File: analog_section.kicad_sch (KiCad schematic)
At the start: 41 parts, among them J1 Probe +, J2 Probe +, J3 Probe +, J4 Probe +, U1 AD9833xRM, U2 LMH6644MTX, U3 TLV75733PDBV, U4 LMH6643MMX, Y2 25MHz

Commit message: Did some routing
Commiting before changing display from i2c to spi
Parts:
- removed JP3: Jumper_3_Bridged12, Connector_PinHeader_2.54mm:PinHeader_1x03_P2.54mm_Vertical, symbol Jumper:Jumper_3_Bridged12
- removed TP13: TestPoint, TestPoint:TestPoint_Keystone_5000-5004_Miniature, symbol Connector:TestPoint
- removed U3: TLV75733PDBV, Package_TO_SOT_SMD:SOT-23-5, symbol Regulator_Linear:TLV75733PDBV
- added C19: 10n, Capacitor_SMD:C_0603_1608Metric, symbol Device:C
- added JP1: Jumper_2_Open, Connector_PinHeader_2.54mm:PinHeader_1x02_P2.54mm_Vertical, symbol Jumper:Jumper_2_Open
- added R1: 100, Resistor_SMD:R_0603_1608Metric, symbol Device:R
- added R21, R22, R23: 10k, Resistor_SMD:R_0603_1608Metric, symbol Device:R
- added U1: TLV757P, Package_TO_SOT_SMD:SOT-23-5, symbol CustomSymbols:TLV757P
- renumbered C9 to C1, C25 to C15, C1 to C16, C10 to C30, C13 to C31, C14 to C32, C11 to C33, C12 to C34, C15 to C35, C5 to C4, C4 to C5, C8 to C6, D3 to D1, D4 to D2, D2 to D3, J1 to J2, J2 to J3, J3 to J4, J4 to J5, PS2 to PS1, R11 to R10, R13 to R11, R14 to R12, R1 to R2, R2 to R3, R3 to R4, R12 to R9, TP2 to TP1, TP11 to TP2, TP8 to TP3, TP7 to TP4, U1 to U2, U2 to U6, Y2 to Y1
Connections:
- net TST_OP_IN is gone; now on net DDS_HPF: U4.5 (+)
- net +3V3A: now also JP1.2 (B), U1.5 (OUT)
- net +5V: now also U1.1 (IN), U1.3 (EN)
- net DDS_AMPLIFIED: now also U4.7; no longer U4.1
- net DDS_HPF: now also JP1.1 (A); no longer U4.3 (+)
- net DDS_OUT: now also R1.1; no longer C16.1
- net GND: now also C19.2, R21.1, R22.1, R23.1, U1.2 (GND), U1.4 (NC)
- net RANGE_S0: now also R22.2
- net RANGE_S1: now also R21.2
- net TEST_GAIN_S: now also R23.2
- net INV: now reaches R3.1, R4.2
- net INV: now also U4.6 (-); no longer U4.2 (-)
- removed net TST_OP_OUT: U4.6 (-), U4.7
- new net DDS_LPF_1: C19.1, R1.2, U4.3 (+)
- new net DDS_LPF_2: C16.1, U4.1, U4.2 (-)
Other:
- note added: "LPF to remove noise fc = 159KHz"
- note added: "There are some digital signals for the range resistors and DDS that need to be present in the analog section. However, crosstalk should not be an issue even for close analog and digital traces. This is because the digital traces do not need to change level when the DDS output is on."
- note added: "This jumper can be used to test the output impedance of the amplifier by measuring open circuit vs load voltage at the output"
- note removed: "This opamp can be used to find the output impedance by measuring open circuit vs load voltage at test point"
- moved on the sheet: C1, C15, C16, C2, C3, C4, C5, C6, PS1, R2, R3, R4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

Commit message: Done
Schematics and PCB are "done".
Meaning I've just finished but need to review
the design before it's ready to order.
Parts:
- renumbered R12 to R10, R15 to R13, R21 to R15, R22 to R16, R23 to R17, R9 to R7, R10 to R8, R11 to R9, TP2 to TP4, TP3 to TP5, TP4 to TP6
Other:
- note added: "Analog Power"
- note added: "Opamp Power Suppy Connections"
- note added: "Resistor Switch Pulldowns"
- note removed: "Analog Power Supplies"
- note removed: "There are some digital signals for the range resistors and DDS that need to be present in the analog section. However, crosstalk should not be an issue even for close analog and digital traces. This is because the digital traces do not need to change level when the DDS output is on."
- moved on the sheet: C30, C31, C32, C33, C34, C35, C4, C5, D1, D2, D3, J2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

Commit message: Added polish
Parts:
- added C44: 10u, Capacitor_SMD:C_0603_1608Metric, symbol Device:C
- added C45: 4u7, Capacitor_SMD:C_0603_1608Metric, symbol Device:C
- added D1, D2: LED, LED_SMD:LED_0603_1608Metric, symbol Device:LED
- added R5, R7: 1k, Resistor_SMD:R_0603_1608Metric, symbol Device:R
- J4, J5: value Probe + -> Probe -
- renumbered C15 to C17, C16 to C18, C19 to C21, C34 to C33, C35 to C34, C33 to C35, D1 to D3, D2 to D4, D3 to D5, R15 to R10, R16 to R11, R17 to R12, R8 to R13, R9 to R14, R10 to R16, R13 to R18, R7 to R9
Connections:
- net +3V3A: now also D1.2 (A)
- net +5V: now also C45.1
- net -3V3A: now also C44.1, R7.2
- net GND: now also C44.2, C45.2, D2.2 (A), R5.2
- new net: D1.1 (K), R5.1
- new net: D2.1 (K), R7.1
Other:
- note added: "Don't bother with LPF for digital signals into analog section. Because the digital signals are constant while the DDS outputs the test waveform and the MCU reads samples."
- moved on the sheet: C31, C32, C33, C34, PS1, R10, R11, R12, U4C, U6E

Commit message: Changed range resistor selector design
Changed range resistor selector from an analog mux
to a MOSFET BPS design. This should improve on resistance, linearity,
and temperature stability for the range resistors.
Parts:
- added C29, C40: 1u, Capacitor_SMD:C_0603_1608Metric, symbol Device:C
- added C38, C39: 100n, Capacitor_SMD:C_0603_1608Metric, symbol Device:C
- added C48: 4u7, Capacitor_SMD:C_0603_1608Metric, symbol Device:C
- added PS2: A0512S-1WR2, Converter_DCDC:Converter_DCDC_XP_POWER-IAxxxxS_THT, symbol Converter_DCDC:IA2412S
- added R23, R26: 10k, Resistor_SMD:R_0603_1608Metric, symbol Device:R
- added U9: LM324, Package_SO:SOIC-14_3.9x8.7mm_P1.27mm, symbol Device:Opamp_Quad
- D1, D2: Already Have (none) -> 1
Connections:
- net RANGE_S1 is gone; now on net RANGE_S0: R10.2
- net +3V3: now also R23.2
- net +5V: now also C48.1, PS2.1 (+Vin)
- net GND: now also C29.2, C38.1, C39.2, C40.1, C48.2, PS2.2 (-Vin), PS2.5 (0V), R26.1, U9.12 (+)
- net RANGE_S0: now also U9.10 (+), U9.5 (+)
- net TEST_GAIN_S: now also U9.3 (+)
- new net: U9.13 (-), U9.14
- new net +12V: C29.1, C38.2, PS2.6 (+Vout), U9.4 (V+)
- new net -12V: C39.1, C40.2, PS2.4 (-Vout), U9.11 (V-)
- new net COMP_REF: R23.1, R26.2, U9.2 (-), U9.6 (-), U9.9 (-)
- new net RANGE_G0: U9.7
- new net RANGE_G1: U9.8
- new net TEST_GAIN_G: U9.1
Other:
- sheet Gain Selector ports: added G0; removed S
- sheet Range Resistor 1 ports: added G0, G1; removed S0, S1
- sheet Range Resistor 2 ports: added G0, G1; removed S0, S1
- note added: "Component selection was based on what's cheap. If this were a real lab instrument it should probably use components that don't change with temperature (atleast in the test signal path). Bad tolerances are OK, since the device needs calibration anyway."
- note added: "Range Resistor BPS Gate Driving"
- note removed: "Resistor Switch Pulldowns"
- moved on the sheet: C1, C17, C18, C2, C21, C3, C30, C31, C32, C33, C34, C35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

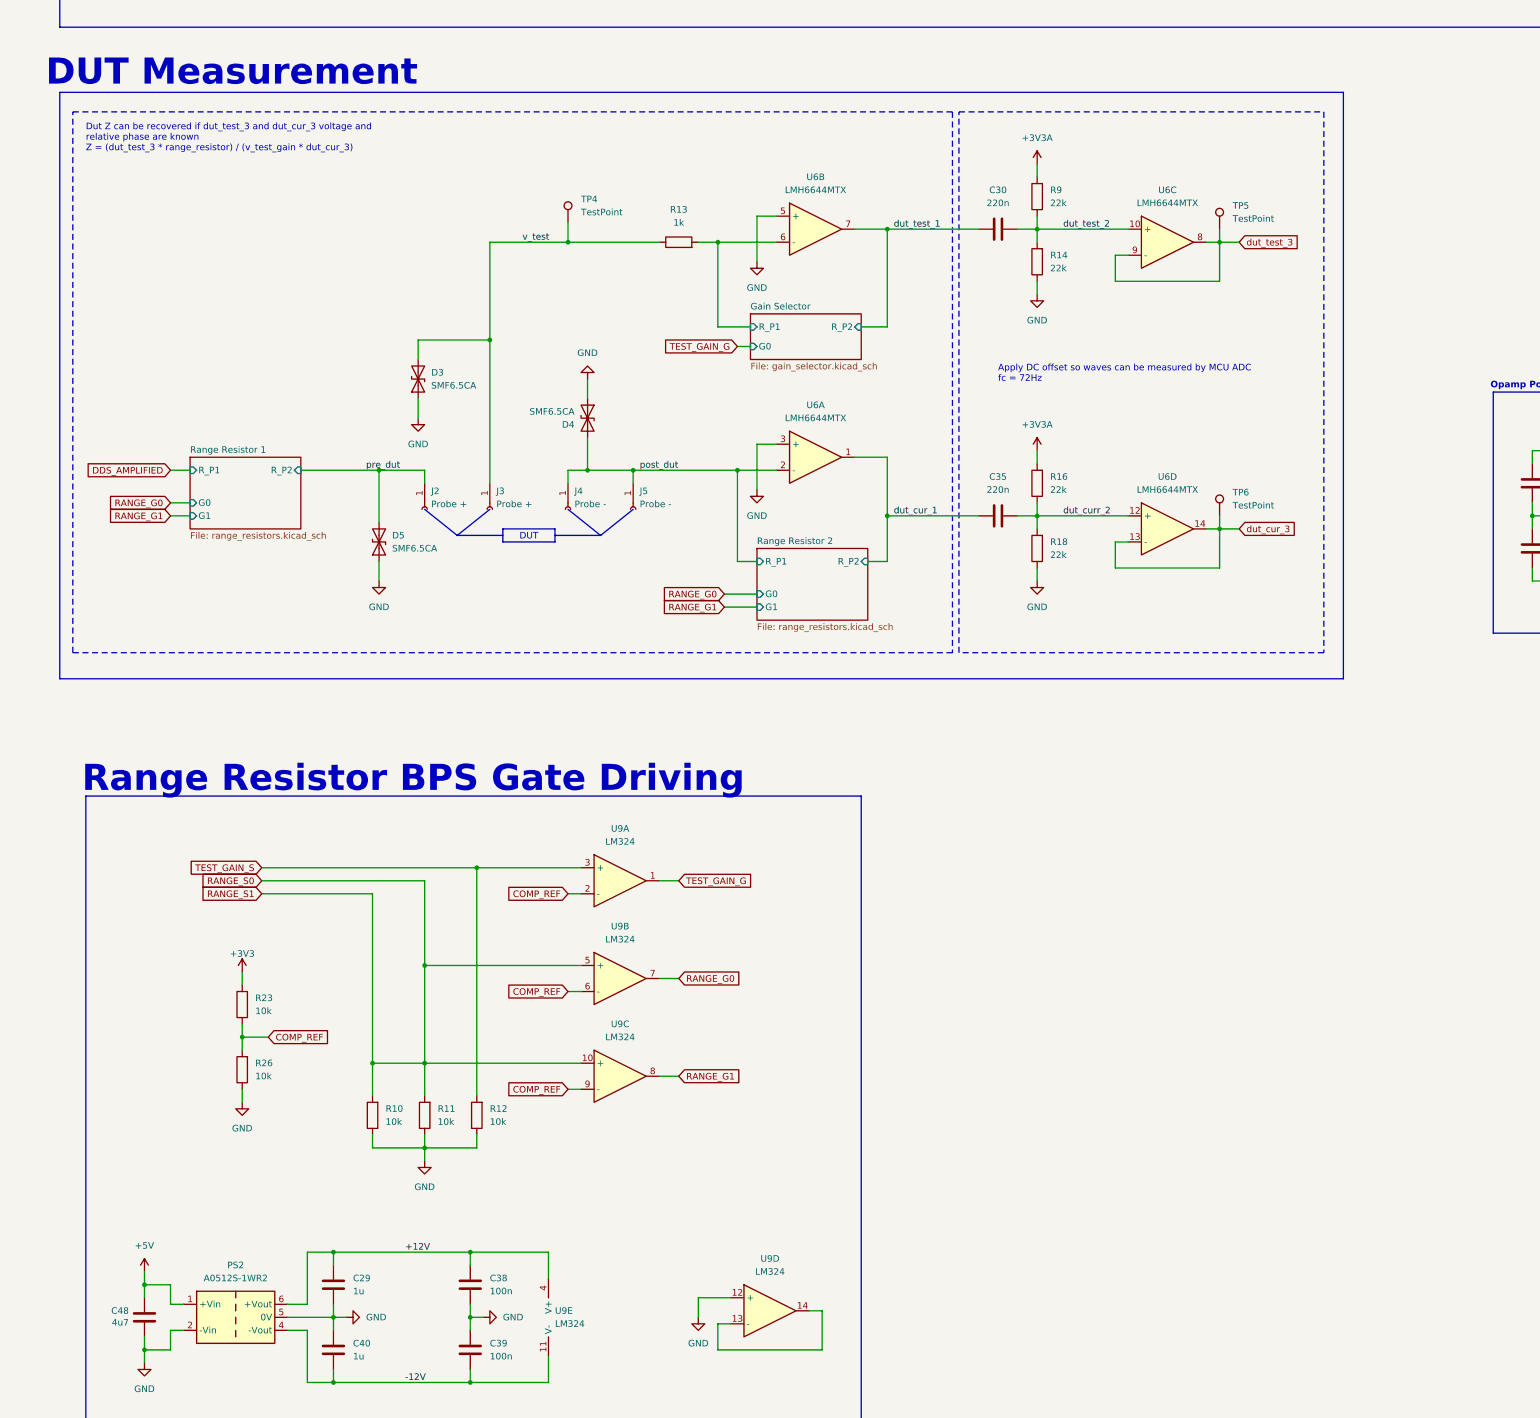
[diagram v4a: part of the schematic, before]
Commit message: Started new layout
Range resistors now use MOSFET BPS.
Currently there's no protection for over voltage on the opamp or mcu
inputs, so that needs to be done.
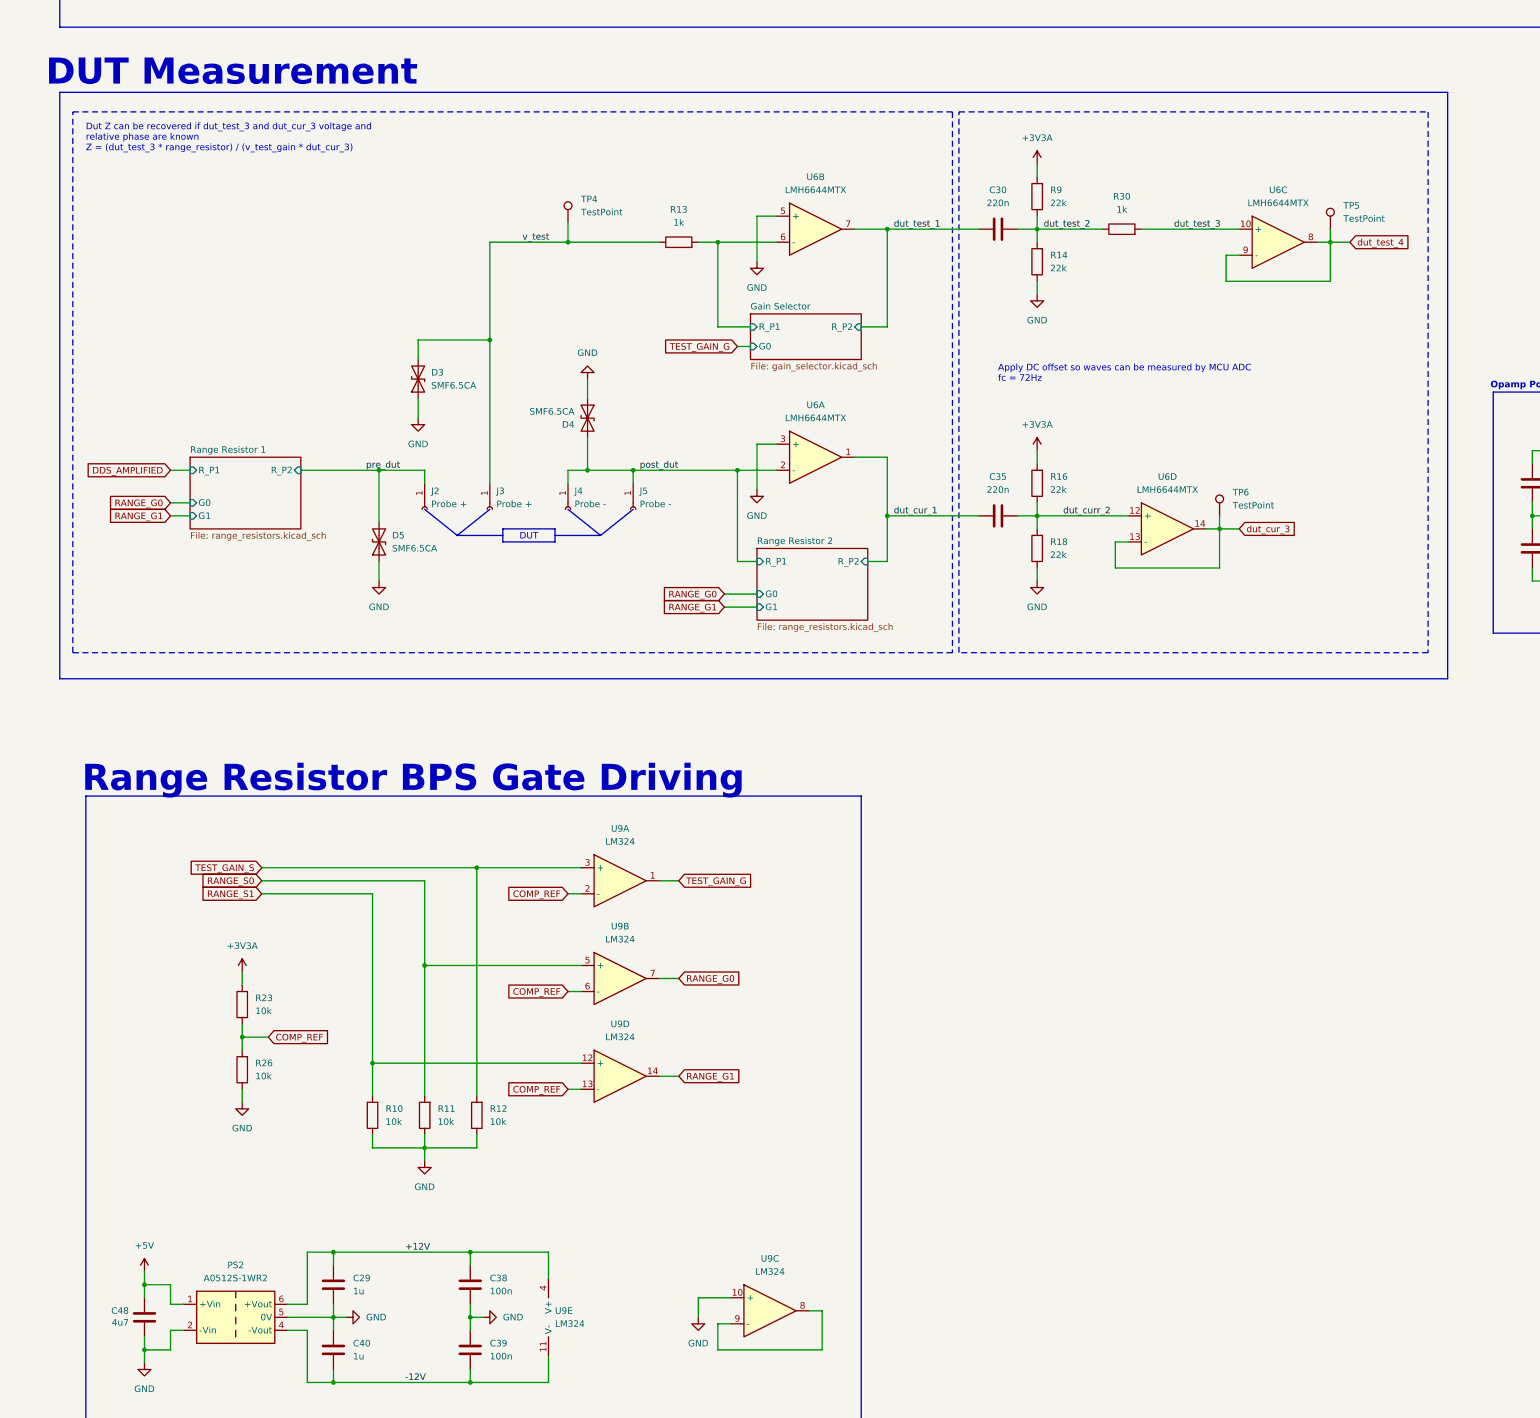
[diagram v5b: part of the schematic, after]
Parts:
- added R30: 1k, Resistor_SMD:R_0603_1608Metric, symbol Device:R
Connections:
- net +3V3: no longer R23.2
- net +3V3A: now also R23.2
- net COMP_REF: now also U9.13 (-); no longer U9.9 (-)
- net GND: now also U9.10 (+); no longer U9.12 (+)
- net RANGE_G1: now also U9.14; no longer U9.8
- net RANGE_S0: no longer R10.2, U9.10 (+)
- net dut_test_2: now also R30.1; no longer U6.10 (+)
- net dut_test_3: now also U6.10 (+), R30.2; no longer TP5.1, U6.8, U6.9 (-)
- new net: U9.8, U9.9 (-)
- new net RANGE_S1: R10.2, U9.12 (+)
- new net dut_test_4: TP5.1, U6.8, U6.9 (-)
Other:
- moved on the sheet: TP5, U6C

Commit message: Added protection to MCU analog inputs
DUT and test voltages now use clamping diodes to protect the MCU from
voltages less than 0V and greater than 3.3V.
Started laying out again, but thinking of trying something different
with the layou of the range resistors around the 1st opamp.
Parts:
- removed R30: 1k, Resistor_SMD:R_0603_1608Metric, symbol Device:R
- removed U6: LMH6644MTX, Package_SO:TSSOP-14_4.4x5mm_P0.65mm, symbol Device:Opamp_Quad
- added C35: 10u, Capacitor_SMD:C_0603_1608Metric, symbol Device:C
- added C36, C40: 100n, Capacitor_SMD:C_0603_1608Metric, symbol Device:C
- added D3, D4, D7, D9: CUS10S30, Diode_SMD:D_SOD-323F, symbol Device:D_Schottky
- added R12, R17: 100, Resistor_SMD:R_0603_1608Metric, symbol Device:R
- added TP6, TP8: TestPoint, TestPoint:TestPoint_Keystone_5000-5004_Miniature, symbol Connector:TestPoint
- added U6: LMH6643MMX, Package_SO:VSSOP-8_3x3mm_P0.65mm, symbol Device:Opamp_Dual
- added U7: TLV9352IPWR, Package_SO:TSSOP-8_4.4x3mm_P0.65mm, symbol Device:Opamp_Dual
- renumbered C6 to C14, C17 to C19, C18 to C20, C21 to C22, C45 to C23, C44 to C24, C30 to C32, C31 to C33, C32 to C34, C35 to C37, C33 to C38, C34 to C39, C29 to C43, C38 to C44, C48 to C45, C40 to C46, C39 to C47, D3 to D5, D4 to D6, D5 to D8, R13 to R11, R14 to R13, R16 to R15, R23 to R20, R26 to R21, R10 to R22, R11 to R23, R12 to R24, R5 to R6, TP6 to TP7, U9 to U10, U2 to U3
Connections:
- net +3V3A: now also D3.1 (K), D7.1 (K), U6.8 (V+)
- net +5V: now also C35.2, C36.2, U7.8 (V+)
- net -3V3A: now also C40.1, U6.4 (V-), U7.4 (V-)
- net GND: now also C35.1, C36.1, C40.2, D4.2 (A), D9.2 (A), U6.3 (+), U6.5 (+)
- net Gain Selector/R_P1: now also U6.6 (-)
- net dut_cur_1: now also U6.1
- net dut_curr_2: now also U7.5 (+)
- net dut_test_1: now also U6.7
- net dut_test_2: now also U7.3 (+)
- net dut_test_3: now also TP5.1, R12.2, U7.1, U7.2 (-)
- net dut_test_4: now also D3.2 (A), D4.1 (K), R12.1, TP6.1; no longer TP5.1
- net post_dut: now also U6.2 (-)
- net dut_cur_3 renamed dut_curr_3
- net dut_curr_3: now also R17.2, U7.6 (-), U7.7
- new net dut_curr_4: D7.2 (A), D9.1 (K), R17.1, TP8.1
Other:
- note added: "Bias and clamp for ADC"
- note added: "Measuring"
- note added: "TI TLV9352IPWR"
- note added: "This jumper can be used to test the output impedance of the amplifier by measuring open circuit vs load voltage at the output. I can't remember why I need to do that though"
- note removed: "This jumper can be used to test the output impedance of the amplifier by measuring open circuit vs load voltage at the output"
- moved on the sheet: C32, C33, C34, C37, C38, C39, D5, D6, D8, J2, J3, J4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

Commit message: Polished PCB
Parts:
- U3: footprint Package_SO:MSOP-10_3x3mm_P0.5mm -> CustomFootprints:MSOP-10_3x3mm_P0.5mm
- U4, U6: footprint Package_SO:VSSOP-8_3x3mm_P0.65mm -> CustomFootprints:VSSOP-8_3x3mm_P0.65mm
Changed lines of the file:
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@@
 			)
 		)
-		(property "Footprint" "Package_SO:VSSOP-8_3x3mm_P0.65mm"
+		(property "Footprint" "CustomFootprints:VSSOP-8_3x3mm_P0.65mm"
 			(at 361.95 83.82 0)
 			(hide yes)
@@
 			)
 		)
-		(property "Footprint" "Package_SO:VSSOP-8_3x3mm_P0.65mm"
+		(property "Footprint" "CustomFootprints:VSSOP-8_3x3mm_P0.65mm"
 			(at 477.52 219.71 0)
 			(hide yes)
@@
 			)
 		)
-		(property "Footprint" "Package_SO:VSSOP-8_3x3mm_P0.65mm"
+		(property "Footprint" "CustomFootprints:VSSOP-8_3x3mm_P0.65mm"
 			(at 252.73 212.09 0)
 			(hide yes)
@@
 			)
 		)
-		(property "Footprint" "Package_SO:VSSOP-8_3x3mm_P0.65mm"
+		(property "Footprint" "CustomFootprints:VSSOP-8_3x3mm_P0.65mm"
 			(at 252.73 167.64 0)
 			(hide yes)
@@
 			)
 		)
-		(property "Footprint" "Package_SO:VSSOP-8_3x3mm_P0.65mm"
+		(property "Footprint" "CustomFootprints:VSSOP-8_3x3mm_P0.65mm"
 			(at 283.21 81.28 0)
 			(hide yes)
@@
 			)
 		)
-		(property "Footprint" "Package_SO:VSSOP-8_3x3mm_P0.65mm"
+		(property "Footprint" "CustomFootprints:VSSOP-8_3x3mm_P0.65mm"
 			(at 441.96 219.71 0)
 			(hide yes)
@@
 			)
 		)
-		(property "Footprint" "Package_SO:MSOP-10_3x3mm_P0.5mm"
+		(property "Footprint" "CustomFootprints:MSOP-10_3x3mm_P0.5mm"
 			(at 176.53 91.44 0)
 			(hide yes)

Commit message: Added gate drive current limiting resistors
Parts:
- added R21, R24: 100, Resistor_SMD:R_0603_1608Metric, symbol Device:R
- added R22: 2k7, Resistor_SMD:R_0603_1608Metric, symbol Device:R
- C20, C32, C37: LCSC PART # C14663 -> C64705
- C24, C3, C35, C4, C5: Already Have 0 -> 1
- D3, D4, D7, D9: Already Have (none) -> 0
- JP1: now left out of the parts list
- R20: value 10k -> 100; Already Have 1 -> 0; LCSC PART # C25804 -> C105588
- U7: value TLV9352IPWR -> LMH6643MMX; footprint Package_SO:TSSOP-8_4.4x3mm_P0.65mm -> CustomFootprints:VSSOP-8_3x3mm_P0.65mm; Already Have (none) -> 0; LCSC PART # C4367453 -> C478382
- renumbered J2 to J3, J3 to J4, J4 to J5, J5 to J6, R21 to R23, R22 to R25, R23 to R26, R24 to R27
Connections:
- net +12V: now also R22.2
- net +3V3A: no longer R20.2
- net COMP_REF: now also R22.1; no longer R20.1
- net RANGE_G0: now also R21.1; no longer U10.7
- net RANGE_G1: now also R24.1; no longer U10.14
- net TEST_GAIN_G: now also R20.1; no longer U10.1
- new net: R20.2, U10.1
- new net: R24.2, U10.14
- new net: R21.2, U10.7
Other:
- note added: "2.55V"
- note added: "This jumper can be used to test the output impedance of the amplifier by measuring open circuit vs load voltage at the output."
- note removed: "TI TLV9352IPWR"
- note removed: "This jumper can be used to test the output impedance of the amplifier by measuring open circuit vs load voltage at the output. I can't remember why I need to do that though"
